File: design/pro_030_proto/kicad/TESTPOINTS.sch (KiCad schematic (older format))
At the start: 4 parts, among them J4 Conn_02x16_Odd_Even, J5 Conn_02x16_Odd_Even, J6 Conn_02x16_Odd_Even, J7 Conn_02x08_Odd_Even

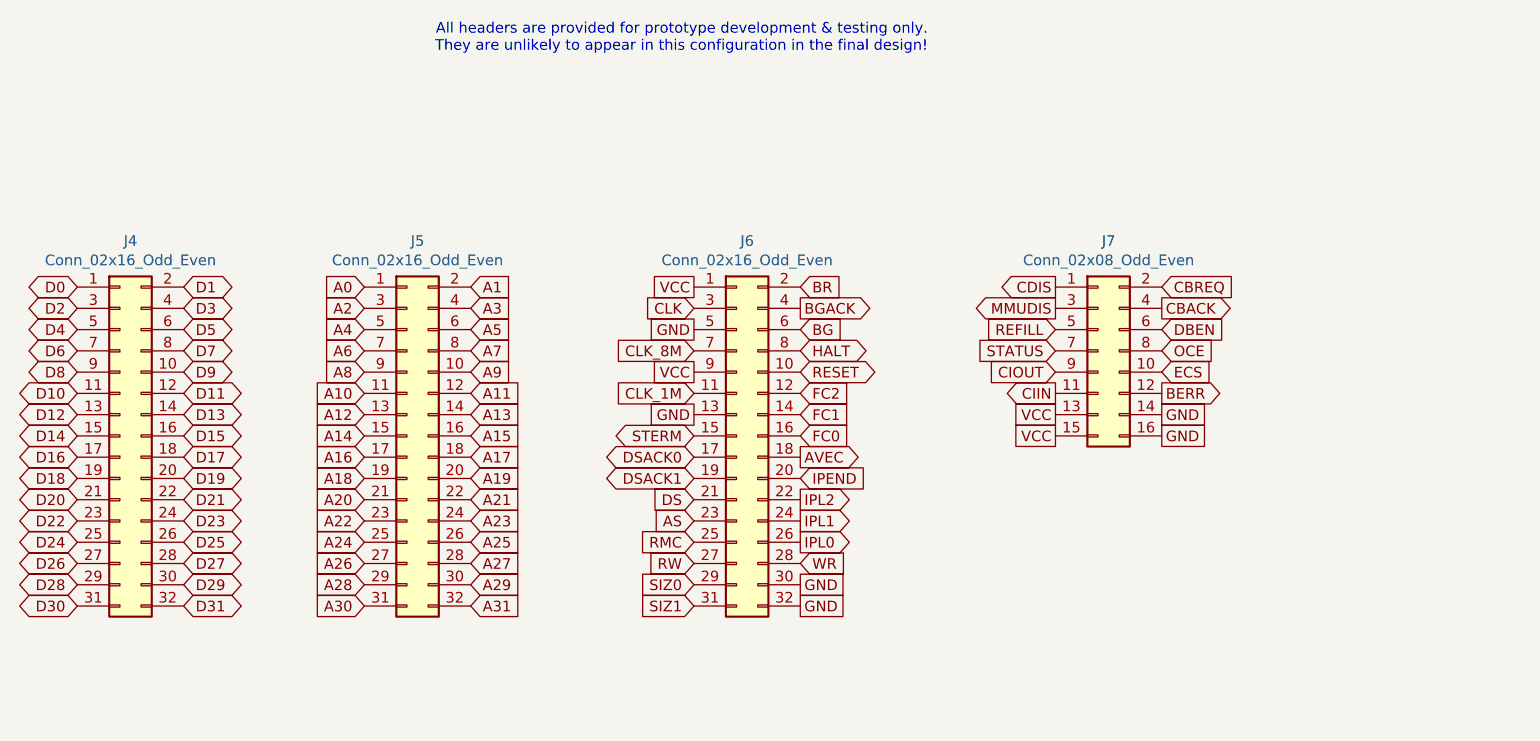
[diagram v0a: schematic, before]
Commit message: Interrupts + Xosera schematic, re-annotate
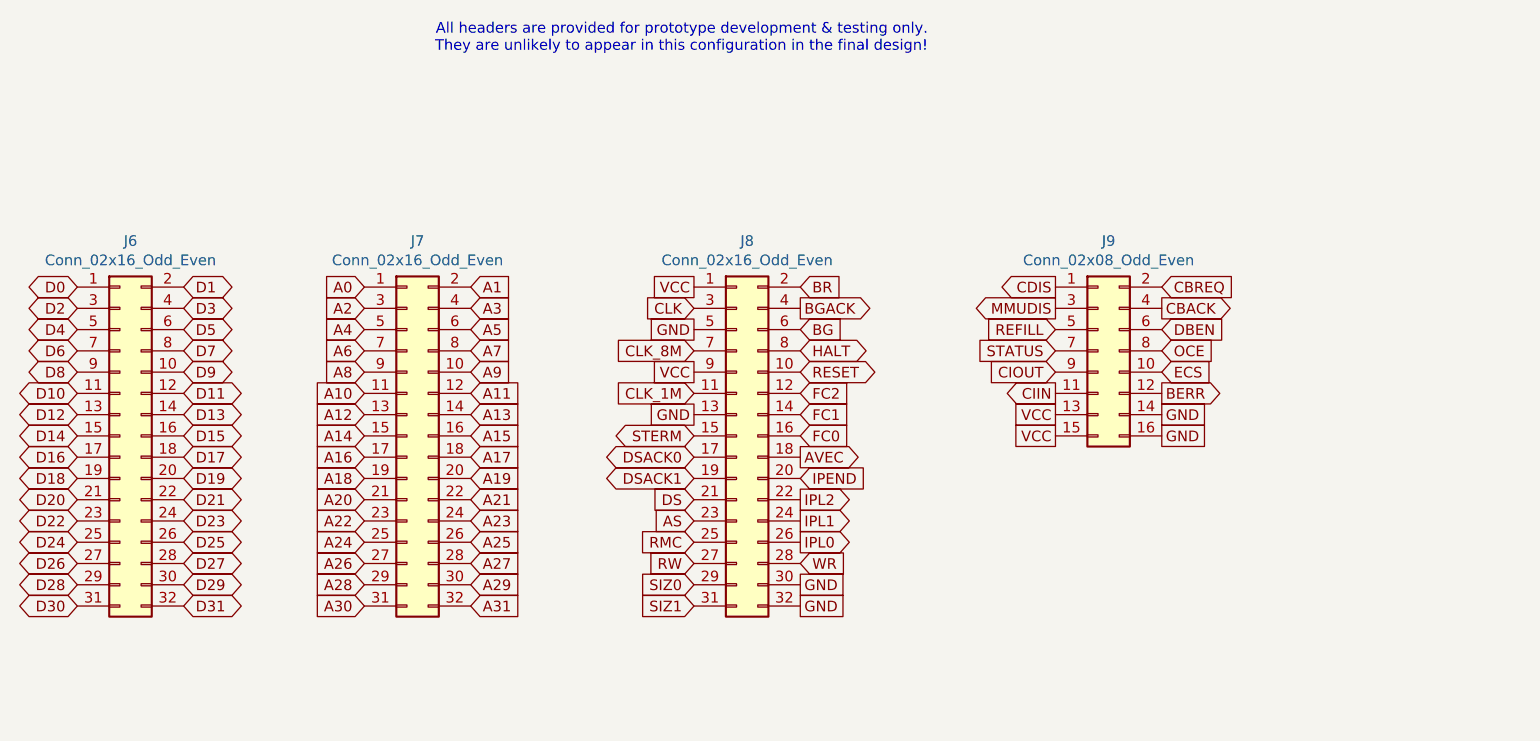
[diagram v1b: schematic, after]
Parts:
- renumbered J4 to J6, J5 to J7, J6 to J8, J7 to J9
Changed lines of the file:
@@
 $Descr A4 11693 8268
 encoding utf-8
-Sheet 10 10
+Sheet 10 13
 Title "rosco_m68k Pro (030) Prototype"
 Date "2021-07-24"
@@
 $EndDescr
 $Comp
-L Connector_Generic:Conn_02x16_Odd_Even J4
+L Connector_Generic:Conn_02x16_Odd_Even J6
 U 1 1 61302767
 P 3500 3700
-F 0 "J4" H 3550 4617 50  0000 C CNN
+F 0 "J6" H 3550 4617 50  0000 C CNN
 F 1 "Conn_02x16_Odd_Even" H 3550 4526 50  0000 C CNN
 F 2 "Connector_PinHeader_2.54mm:PinHeader_2x16_P2.54mm_Vertical" H 3500 3700 50  0001 C CNN
@@
 $EndComp
 $Comp
-L Connector_Generic:Conn_02x16_Odd_Even J5
+L Connector_Generic:Conn_02x16_Odd_Even J7
 U 1 1 6130437C
 P 4850 3700
-F 0 "J5" H 4900 4617 50  0000 C CNN
+F 0 "J7" H 4900 4617 50  0000 C CNN
 F 1 "Conn_02x16_Odd_Even" H 4900 4526 50  0000 C CNN
 F 2 "Connector_PinHeader_2.54mm:PinHeader_2x16_P2.54mm_Vertical" H 4850 3700 50  0001 C CNN
@@
 A31
 $Comp
-L Connector_Generic:Conn_02x16_Odd_Even J6
+L Connector_Generic:Conn_02x16_Odd_Even J8
 U 1 1 6131D7DE
 P 6400 3700
-F 0 "J6" H 6450 4617 50  0000 C CNN
+F 0 "J8" H 6450 4617 50  0000 C CNN
 F 1 "Conn_02x16_Odd_Even" H 6450 4526 50  0000 C CNN
 F 2 "Connector_PinHeader_2.54mm:PinHeader_2x16_P2.54mm_Vertical" H 6400 3700 50  0001 C CNN
@@
 GND
 $Comp
-L Connector_Generic:Conn_02x08_Odd_Even J7
+L Connector_Generic:Conn_02x08_Odd_Even J9
 U 1 1 6132B041
 P 8100 3300
-F 0 "J7" H 8150 3817 50  0000 C CNN
+F 0 "J9" H 8150 3817 50  0000 C CNN
 F 1 "Conn_02x08_Odd_Even" H 8150 3726 50  0000 C CNN
 F 2 "Connector_PinHeader_2.54mm:PinHeader_2x08_P2.54mm_Vertical" H 8100 3300 50  0001 C CNN

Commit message: Finally fix ERC...
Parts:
- added J18: Conn_02x08_Male, Connector_PinHeader_2.54mm:PinHeader_2x08_P2.54mm_Vertical, symbol Connector_Generic:Conn_02x08_Odd_Even
- added J19: Conn_02x02_Odd_Even, Connector_PinHeader_2.54mm:PinHeader_2x02_P2.54mm_Vertical, symbol Connector_Generic:Conn_02x02_Odd_Even
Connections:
- net GND: now also J18.15 (Pin_15), J19.2 (Pin_2), J19.4 (Pin_4)
- new net ANYIACK: J18.16 (Pin_16)
- new net IACK1: J18.2 (Pin_2)
- new net IACK2: J18.4 (Pin_4)
- new net IACK3: J18.6 (Pin_6)
- new net IACK4: J18.8 (Pin_8)
- new net IACK5: J18.10 (Pin_10)
- new net IACK6: J18.12 (Pin_12)
- new net IACK7: J18.14 (Pin_14)
- new net IRQ1: J18.1 (Pin_1)
- new net IRQ2: J18.3 (Pin_3)
- new net IRQ3: J18.5 (Pin_5)
- new net IRQ4: J18.7 (Pin_7)
- new net IRQ5: J18.9 (Pin_9)
- new net IRQ6: J18.11 (Pin_11)
- new net IRQ7: J18.13 (Pin_13)
- new net LV_R: J19.1 (Pin_1)
- new net LV_W: J19.3 (Pin_3)
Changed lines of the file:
@@
 Text Notes 7300 1900 2    50   ~ 0
 All headers are provided for prototype development & testing only.\nThey are unlikely to appear in this configuration in the final design!
+$Comp
+L Connector_Generic:Conn_02x08_Odd_Even J18
+U 1 1 6169B008
+P 8250 4600
+F 0 "J18" H 8300 5117 50  0000 C CNN
+F 1 "Conn_02x08_Male" H 8300 5026 50  0000 C CNN
+F 2 "Connector_PinHeader_2.54mm:PinHeader_2x08_P2.54mm_Vertical" H 8250 4600 50  0001 C CNN
+F 3 "~" H 8250 4600 50  0001 C CNN
+	1    8250 4600
+	1    0    0    -1
+$EndComp
+Text GLabel 8550 4300 2    50   Input ~ 0
+IACK1
+Text GLabel 8550 4400 2    50   Input ~ 0
+IACK2
+Text GLabel 8550 4500 2    50   Input ~ 0
+IACK3
+Text GLabel 8550 4600 2    50   Input ~ 0
+IACK4
+Text GLabel 8550 4700 2    50   Input ~ 0
+IACK5
+Text GLabel 8550 4800 2    50   Input ~ 0
+IACK6
+Text GLabel 8550 4900 2    50   Input ~ 0
+IACK7
+Text GLabel 8550 5000 2    50   Input ~ 0
+ANYIACK
+$Comp
+L Connector_Generic:Conn_02x02_Odd_Even J19
+U 1 1 616A9AD9
+P 9500 3000
+F 0 "J19" H 9550 3217 50  0000 C CNN
+F 1 "Conn_02x02_Odd_Even" H 9550 3126 50  0000 C CNN
+F 2 "Connector_PinHeader_2.54mm:PinHeader_2x02_P2.54mm_Vertical" H 9500 3000 50  0001 C CNN
+F 3 "~" H 9500 3000 50  0001 C CNN
+	1    9500 3000
+	1    0    0    -1
+$EndComp
+Text GLabel 9300 3000 0    50   Output ~ 0
+LV_R
+Text GLabel 9300 3100 0    50   Output ~ 0
+LV_W
+Text GLabel 9800 3000 2    50   UnSpc ~ 0
+GND
+Text GLabel 9800 3100 2    50   UnSpc ~ 0
+GND
+Text GLabel 8050 4300 0    50   3State ~ 0
+IRQ1
+Text GLabel 8050 4400 0    50   3State ~ 0
+IRQ2
+Text GLabel 8050 4500 0    50   3State ~ 0
+IRQ3
+Text GLabel 8050 4600 0    50   3State ~ 0
+IRQ4
+Text GLabel 8050 4700 0    50   3State ~ 0
+IRQ5
+Text GLabel 8050 4800 0    50   3State ~ 0
+IRQ6
+Text GLabel 8050 4900 0    50   3State ~ 0
+IRQ7
+Text GLabel 8050 5000 0    50   UnSpc ~ 0
+GND
 $EndSCHEMATC

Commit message: Lots more changes
* Add DIN expansion connectors (provisional pinout)
* Fix incorrect address lines for RAM & ROM (Doh!)
* Remove unused level shifters
* Fix clock enables
* Lots of other small fixes
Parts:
- removed J19: Conn_02x02_Odd_Even, Connector_PinHeader_2.54mm:PinHeader_2x02_P2.54mm_Vertical, symbol Connector_Generic:Conn_02x02_Odd_Even
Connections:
- net A0: now also J6.2 (Pin_2); no longer J7.1 (Pin_1)
- net A1: now also J6.4 (Pin_4); no longer J7.2 (Pin_2)
- net A10: now also J6.22 (Pin_22); no longer J7.11 (Pin_11)
- net A11: now also J6.24 (Pin_24); no longer J7.12 (Pin_12)
- net A12: now also J6.26 (Pin_26); no longer J7.13 (Pin_13)
- net A13: now also J6.28 (Pin_28); no longer J7.14 (Pin_14)
- net A14: now also J6.30 (Pin_30); no longer J7.15 (Pin_15)
- net A15: now also J6.32 (Pin_32); no longer J7.16 (Pin_16)
- net A16: now also J7.2 (Pin_2); no longer J7.17 (Pin_17)
- net A17: now also J7.4 (Pin_4); no longer J7.18 (Pin_18)
- net A18: now also J7.6 (Pin_6); no longer J7.19 (Pin_19)
- net A19: now also J7.8 (Pin_8); no longer J7.20 (Pin_20)
- net A2: now also J6.6 (Pin_6); no longer J7.3 (Pin_3)
- net A20: now also J7.10 (Pin_10); no longer J7.21 (Pin_21)
- net A21: now also J7.12 (Pin_12); no longer J7.22 (Pin_22)
- net A22: now also J7.14 (Pin_14); no longer J7.23 (Pin_23)
- net A23: now also J7.16 (Pin_16); no longer J7.24 (Pin_24)
- net A24: now also J7.18 (Pin_18); no longer J7.25 (Pin_25)
- net A25: now also J7.20 (Pin_20); no longer J7.26 (Pin_26)
- net A26: now also J7.22 (Pin_22); no longer J7.27 (Pin_27)
- net A27: now also J7.24 (Pin_24); no longer J7.28 (Pin_28)
- net A28: now also J7.26 (Pin_26); no longer J7.29 (Pin_29)
- net A29: now also J7.28 (Pin_28); no longer J7.30 (Pin_30)
- net A3: now also J6.8 (Pin_8); no longer J7.4 (Pin_4)
- net A30: now also J7.30 (Pin_30); no longer J7.31 (Pin_31)
- net A4: now also J6.10 (Pin_10); no longer J7.5 (Pin_5)
- net A5: now also J6.12 (Pin_12); no longer J7.6 (Pin_6)
- net A6: now also J6.14 (Pin_14); no longer J7.7 (Pin_7)
- net A7: now also J6.16 (Pin_16); no longer J7.8 (Pin_8)
- net A8: now also J6.18 (Pin_18); no longer J7.9 (Pin_9)
- net A9: now also J6.20 (Pin_20); no longer J7.10 (Pin_10)
- net BGACK: now also J8.8 (Pin_8); no longer J8.4 (Pin_4)
- net BR: now also J8.10 (Pin_10); no longer J8.2 (Pin_2)
- net D1: now also J6.3 (Pin_3); no longer J6.2 (Pin_2)
- net D10: now also J6.21 (Pin_21); no longer J6.11 (Pin_11)
- net D11: now also J6.23 (Pin_23); no longer J6.12 (Pin_12)
- net D12: now also J6.25 (Pin_25); no longer J6.13 (Pin_13)
- net D13: now also J6.27 (Pin_27); no longer J6.14 (Pin_14)
- net D14: now also J6.29 (Pin_29); no longer J6.15 (Pin_15)
- net D15: now also J6.31 (Pin_31); no longer J6.16 (Pin_16)
- net D16: now also J7.1 (Pin_1); no longer J6.17 (Pin_17)
- net D17: now also J7.3 (Pin_3); no longer J6.18 (Pin_18)
- net D18: now also J7.5 (Pin_5); no longer J6.19 (Pin_19)
- net D19: now also J7.7 (Pin_7); no longer J6.20 (Pin_20)
- net D2: now also J6.5 (Pin_5); no longer J6.3 (Pin_3)
- net D20: now also J7.9 (Pin_9); no longer J6.21 (Pin_21)
- net D21: now also J7.11 (Pin_11); no longer J6.22 (Pin_22)
- net D22: now also J7.13 (Pin_13); no longer J6.23 (Pin_23)
- net D23: now also J7.15 (Pin_15); no longer J6.24 (Pin_24)
- net D24: now also J7.17 (Pin_17); no longer J6.25 (Pin_25)
- net D25: now also J7.19 (Pin_19); no longer J6.26 (Pin_26)
- net D26: now also J7.21 (Pin_21); no longer J6.27 (Pin_27)
- net D27: now also J7.23 (Pin_23); no longer J6.28 (Pin_28)
- net D28: now also J7.25 (Pin_25); no longer J6.29 (Pin_29)
- net D29: now also J7.27 (Pin_27); no longer J6.30 (Pin_30)
- net D3: now also J6.7 (Pin_7); no longer J6.4 (Pin_4)
- net D30: now also J7.29 (Pin_29); no longer J6.31 (Pin_31)
- net D31: now also J7.31 (Pin_31); no longer J6.32 (Pin_32)
- net D4: now also J6.9 (Pin_9); no longer J6.5 (Pin_5)
- net D5: now also J6.11 (Pin_11); no longer J6.6 (Pin_6)
- net D6: now also J6.13 (Pin_13); no longer J6.7 (Pin_7)
- net D7: now also J6.15 (Pin_15); no longer J6.8 (Pin_8)
- net D8: now also J6.17 (Pin_17); no longer J6.9 (Pin_9)
- net D9: now also J6.19 (Pin_19); no longer J6.10 (Pin_10)
- net FC0: now also J8.12 (Pin_12); no longer J8.16 (Pin_16)
- net FC2: now also J8.16 (Pin_16); no longer J8.12 (Pin_12)
- net HALT: now also J8.4 (Pin_4); no longer J8.8 (Pin_8)
- net RESET: now also J8.2 (Pin_2); no longer J8.10 (Pin_10)
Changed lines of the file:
@@
 $Descr A4 11693 8268
 encoding utf-8
-Sheet 10 15
+Sheet 10 14
 Title "rosco_m68k Pro (030) Prototype"
 Date "2021-10-01"
@@
 Text GLabel 3300 3000 0    50   BiDi ~ 0
 D0
+Text GLabel 3300 3200 0    50   BiDi ~ 0
+D2
+Text GLabel 3300 3400 0    50   BiDi ~ 0
+D4
+Text GLabel 3300 3600 0    50   BiDi ~ 0
+D6
+Text GLabel 3300 3800 0    50   BiDi ~ 0
+D8
+Text GLabel 3300 4000 0    50   BiDi ~ 0
+D10
+Text GLabel 3300 4200 0    50   BiDi ~ 0
+D12
+Text GLabel 3300 4400 0    50   BiDi ~ 0
+D14
+Text GLabel 4650 3000 0    50   BiDi ~ 0
+D16
+Text GLabel 4650 3200 0    50   BiDi ~ 0
+D18
+Text GLabel 4650 3400 0    50   BiDi ~ 0
+D20
+Text GLabel 4650 3600 0    50   BiDi ~ 0
+D22
+Text GLabel 4650 3800 0    50   BiDi ~ 0
+D24
+Text GLabel 4650 4000 0    50   BiDi ~ 0
+D26
+Text GLabel 4650 4200 0    50   BiDi ~ 0
+D28
+Text GLabel 4650 4400 0    50   BiDi ~ 0
+D30
 Text GLabel 3300 3100 0    50   BiDi ~ 0
-D2
-Text GLabel 3300 3200 0    50   BiDi ~ 0
-D4
+D1
 Text GLabel 3300 3300 0    50   BiDi ~ 0
-D6
-Text GLabel 3300 3400 0    50   BiDi ~ 0
-D8
+D3
 Text GLabel 3300 3500 0    50   BiDi ~ 0
-D10
-Text GLabel 3300 3600 0    50   BiDi ~ 0
-D12
+D5
 Text GLabel 3300 3700 0    50   BiDi ~ 0
-D14
-Text GLabel 3300 3800 0    50   BiDi ~ 0
-D16
+D7
 Text GLabel 3300 3900 0    50   BiDi ~ 0
-D18
-Text GLabel 3300 4000 0    50   BiDi ~ 0
-D20
+D9
 Text GLabel 3300 4100 0    50   BiDi ~ 0
-D22
-Text GLabel 3300 4200 0    50   BiDi ~ 0
-D24
+D11
 Text GLabel 3300 4300 0    50   BiDi ~ 0
-D26
-Text GLabel 3300 4400 0    50   BiDi ~ 0
-D28
+D13
 Text GLabel 3300 4500 0    50   BiDi ~ 0
-D30
-Text GLabel 3800 3000 2    50   BiDi ~ 0
-D1
-Text GLabel 3800 3100 2    50   BiDi ~ 0
-D3
-Text GLabel 3800 3200 2    50   BiDi ~ 0
-D5
-Text GLabel 3800 3300 2    50   BiDi ~ 0
-D7
-Text GLabel 3800 3400 2    50   BiDi ~ 0
-D9
-Text GLabel 3800 3500 2    50   BiDi ~ 0
-D11
-Text GLabel 3800 3600 2    50   BiDi ~ 0
-D13
-Text GLabel 3800 3700 2    50   BiDi ~ 0
 D15
-Text GLabel 3800 3800 2    50   BiDi ~ 0
+Text GLabel 4650 3100 0    50   BiDi ~ 0
 D17
-Text GLabel 3800 3900 2    50   BiDi ~ 0
+Text GLabel 4650 3300 0    50   BiDi ~ 0
 D19
-Text GLabel 3800 4000 2    50   BiDi ~ 0
+Text GLabel 4650 3500 0    50   BiDi ~ 0
 D21
-Text GLabel 3800 4100 2    50   BiDi ~ 0
+Text GLabel 4650 3700 0    50   BiDi ~ 0
 D23
-Text GLabel 3800 4200 2    50   BiDi ~ 0
+Text GLabel 4650 3900 0    50   BiDi ~ 0
 D25
-Text GLabel 3800 4300 2    50   BiDi ~ 0
+Text GLabel 4650 4100 0    50   BiDi ~ 0
 D27
-Text GLabel 3800 4400 2    50   BiDi ~ 0
+Text GLabel 4650 4300 0    50   BiDi ~ 0
 D29
-Text GLabel 3800 4500 2    50   BiDi ~ 0
+Text GLabel 4650 4500 0    50   BiDi ~ 0
 D31
-Text GLabel 4650 3000 0    50   Input ~ 0
+Text GLabel 3800 3000 2    50   Input ~ 0
 A0
-Text GLabel 4650 3100 0    50   Input ~ 0
-A2
-Text GLabel 4650 3200 0    50   Input ~ 0
-A4
-Text GLabel 4650 3300 0    50   Input ~ 0
+Text GLabel 3800 3600 2    50   Input ~ 0
 A6
-Text GLabel 4650 3400 0    50   Input ~ 0
+Text GLabel 3800 3800 2    50   Input ~ 0
 A8
-Text GLabel 4650 3500 0    50   Input ~ 0
+Text GLabel 3800 4000 2    50   Input ~ 0
 A10
-Text GLabel 4650 3600 0    50   Input ~ 0
+Text GLabel 3800 4200 2    50   Input ~ 0
 A12
-Text GLabel 4650 3700 0    50   Input ~ 0
+Text GLabel 3800 4400 2    50   Input ~ 0
 A14
-Text GLabel 4650 3800 0    50   Input ~ 0
+Text GLabel 5150 3000 2    50   Input ~ 0
 A16
-Text GLabel 4650 3900 0    50   Input ~ 0
+Text GLabel 5150 3200 2    50   Input ~ 0
 A18
-Text GLabel 4650 4000 0    50   Input ~ 0
+Text GLabel 5150 3400 2    50   Input ~ 0
 A20
-Text GLabel 4650 4100 0    50   Input ~ 0
+Text GLabel 5150 3600 2    50   Input ~ 0
 A22
-Text GLabel 4650 4200 0    50   Input ~ 0
+Text GLabel 5150 3800 2    50   Input ~ 0
 A24
-Text GLabel 4650 4300 0    50   Input ~ 0
+Text GLabel 5150 4000 2    50   Input ~ 0
 A26
-Text GLabel 4650 4400 0    50   Input ~ 0
+Text GLabel 5150 4200 2    50   Input ~ 0
 A28
-Text GLabel 4650 4500 0    50   Input ~ 0
+Text GLabel 5150 4400 2    50   Input ~ 0
 A30
-Text GLabel 5150 3000 2    50   Input ~ 0
+Text GLabel 3800 3100 2    50   Input ~ 0
 A1
+Text GLabel 3800 3300 2    50   Input ~ 0
+A3
+Text GLabel 3800 3500 2    50   Input ~ 0
+A5
+Text GLabel 3800 3700 2    50   Input ~ 0
+A7
+Text GLabel 3800 3900 2    50   Input ~ 0
+A9
+Text GLabel 3800 4100 2    50   Input ~ 0
+A11
+Text GLabel 3800 4300 2    50   Input ~ 0
+A13
+Text GLabel 3800 4500 2    50   Input ~ 0
+A15
 Text GLabel 5150 3100 2    50   Input ~ 0
-A3
-Text GLabel 5150 3200 2    50   Input ~ 0
-A5
+A17
 Text GLabel 5150 3300 2    50   Input ~ 0
-A7
-Text GLabel 5150 3400 2    50   Input ~ 0
-A9
+A19
 Text GLabel 5150 3500 2    50   Input ~ 0
-A11
-Text GLabel 5150 3600 2    50   Input ~ 0
-A13
+A21
 Text GLabel 5150 3700 2    50   Input ~ 0
-A15
-Text GLabel 5150 3800 2    50   Input ~ 0
-A17
+A23
 Text GLabel 5150 3900 2    50   Input ~ 0
-A19
-Text GLabel 5150 4000 2    50   Input ~ 0
-A21
+A25
 Text GLabel 5150 4100 2    50   Input ~ 0
-A23
-Text GLabel 5150 4200 2    50   Input ~ 0
-A25
+A27
 Text GLabel 5150 4300 2    50   Input ~ 0
-A27
-Text GLabel 5150 4400 2    50   Input ~ 0
 A29
 Text GLabel 5150 4500 2    50   Input ~ 0
@@
 Text GLabel 6700 4300 2    50   Input ~ 0
 WR
-Text GLabel 6700 3000 2    50   Input ~ 0
+Text GLabel 6700 3400 2    50   Input ~ 0
 BR
-Text GLabel 6700 3100 2    50   Output ~ 0
+Text GLabel 6700 3300 2    50   Output ~ 0
 BGACK
 Text GLabel 6700 3200 2    50   Input ~ 0
 BG
-Text GLabel 6700 3300 2    50   BiDi ~ 0
+Text GLabel 6700 3100 2    50   BiDi ~ 0
 HALT
-Text GLabel 6700 3400 2    50   BiDi ~ 0
+Text GLabel 6700 3000 2    50   BiDi ~ 0
 RESET
-Text GLabel 6700 3500 2    50   Input ~ 0
+Text GLabel 6700 3700 2    50   Input ~ 0
 FC2
 Text GLabel 6700 3600 2    50   Input ~ 0
 FC1
-Text GLabel 6700 3700 2    50   Input ~ 0
+Text GLabel 6700 3500 2    50   Input ~ 0
 FC0
 Text GLabel 6700 3800 2    50   Output ~ 0
@@
 Text GLabel 8550 5000 2    50   Input ~ 0
 ANYIACK
-$Comp
-L Connector_Generic:Conn_02x02_Odd_Even J19
-U 1 1 616A9AD9
-P 9500 3000
-F 0 "J19" H 9550 3217 50  0000 C CNN
-F 1 "Conn_02x02_Odd_Even" H 9550 3126 50  0000 C CNN
-F 2 "Connector_PinHeader_2.54mm:PinHeader_2x02_P2.54mm_Vertical" H 9500 3000 50  0001 C CNN
-F 3 "~" H 9500 3000 50  0001 C CNN
-	1    9500 3000
-	1    0    0    -1
-$EndComp
-Text GLabel 9300 3000 0    50   Output ~ 0
-LV_R
-Text GLabel 9300 3100 0    50   Output ~ 0
-LV_W
-Text GLabel 9800 3000 2    50   UnSpc ~ 0
-GND
-Text GLabel 9800 3100 2    50   UnSpc ~ 0
-GND
 Text GLabel 8050 4300 0    50   3State ~ 0
 IRQ1
@@
 Text GLabel 8050 5000 0    50   UnSpc ~ 0
 GND
+Text GLabel 3800 3400 2    50   Input ~ 0
+A4
+Text GLabel 3800 3200 2    50   Input ~ 0
+A2
 $EndSCHEMATC
